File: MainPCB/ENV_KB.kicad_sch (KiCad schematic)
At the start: 198 parts

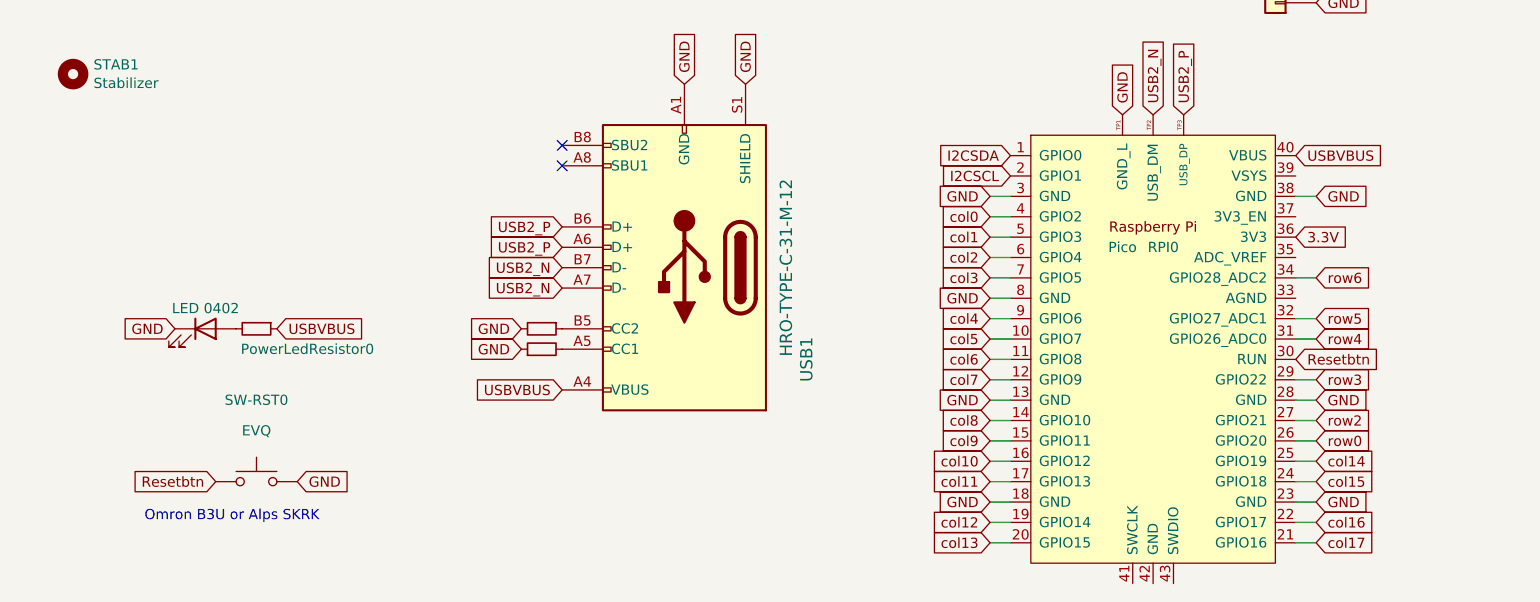
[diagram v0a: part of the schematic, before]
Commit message: swapped footprint of various parts, updated the logo and tweaked some traces
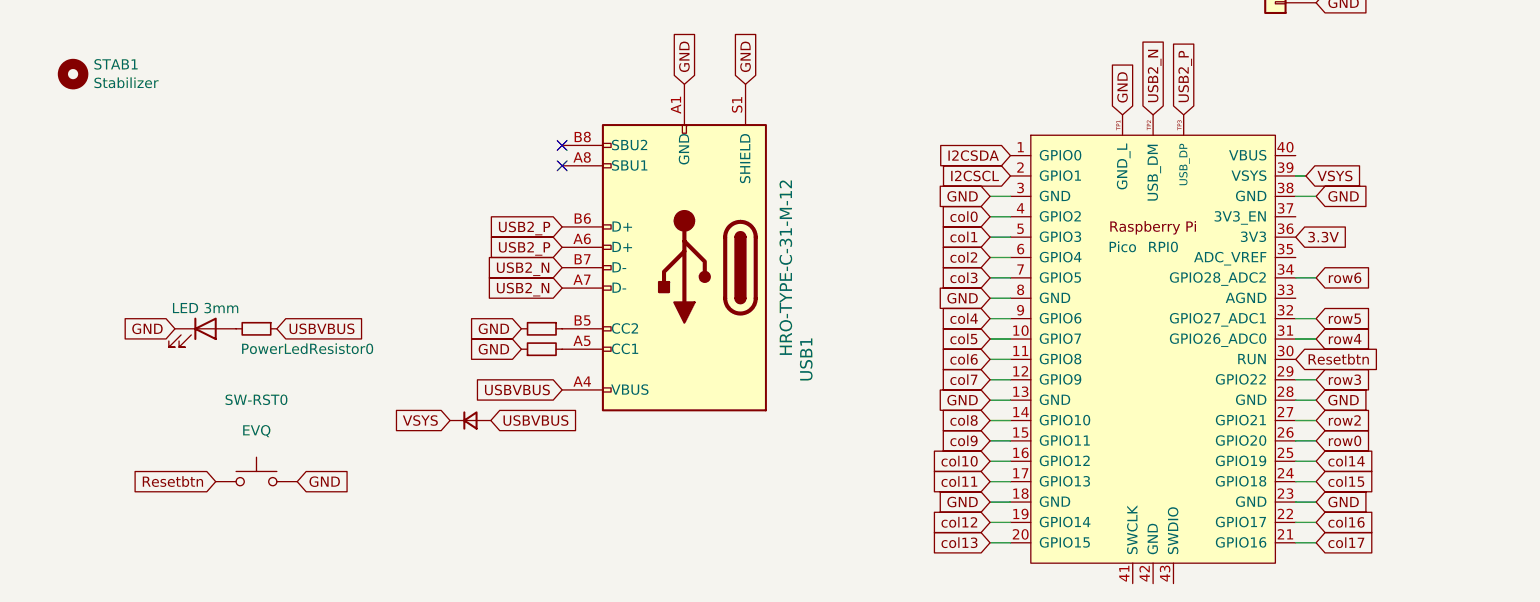
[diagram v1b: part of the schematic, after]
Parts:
- added D89: 1n4002, Diode_THT:D_DO-35_SOD27_P7.62mm_Horizontal, symbol Device:D_Small
- PowerLED0: value LED 0402 -> LED 3mm; footprint LED_SMD:LED_0402_1005Metric -> LED_THT:LED_D3.0mm
- PowerLedResistor0: value 47K Resistor 0402 -> 47K Resistor; footprint Resistor_SMD:R_0402_1005Metric -> Resistor_THT:R_Axial_DIN0207_L6.3mm_D2.5mm_P7.62mm_Horizontal
- RESISTOR0, RESISTOR1: value 5.1kohm 0402 -> 5.1k; footprint Resistor_SMD:R_0402_1005Metric -> Resistor_THT:R_Axial_DIN0207_L6.3mm_D2.5mm_P7.62mm_Horizontal
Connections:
- net USBVBUS: now also D89.2 (A); no longer RPI0.40 (VBUS)
- net VSYS: now reaches RPI0.39 (VSYS)
- net VSYS: now also D89.1 (K)
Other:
- note removed: "Omron B3U or Alps SKRK"
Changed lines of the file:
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@@
     (stroke (width 0) (type default) (color 0 0 0 0))
   )
+  (wire (pts (xy 346.71 233.68) (xy 347.98 233.68))
+    (stroke (width 0) (type default) (color 0 0 0 0))
+  )
   (wire (pts (xy 288.29 181.61) (xy 288.29 182.88))
     (stroke (width 0) (type default) (color 0 0 0 0))
@@
     (effects (font (size 1.27 1.27)) (justify left bottom))
   )
-  (text "Omron B3U or Alps SKRK" (at 203.2 276.86 0)
-    (effects (font (size 1.27 1.27)) (justify left bottom))
-  )
   (global_label "I2CSDA" (shape input) (at 349.25 204.47 0) (fields_autoplaced)
     (effects (font (size 1.27 1.27)) (justify left))
@@
     )
   )
+  (global_label "VSYS" (shape input) (at 347.98 233.68 0) (fields_autoplaced)
+    (effects (font (size 1.27 1.27)) (justify left))
+    (property "Intersheet References" "${INTERSHEET_REFS}" (id 0) (at 354.9004 233.6006 0)
+      (effects (font (size 1.27 1.27)) (justify left) hide)
+    )
+  )
   (global_label "col17" (shape input) (at 477.52 16.51 180) (fields_autoplaced)
     (effects (font (size 1.27 1.27)) (justify right))
@@
     )
   )
+  (global_label "VSYS" (shape input) (at 241.3 264.16 180) (fields_autoplaced)
+    (effects (font (size 1.27 1.27)) (justify right))
+    (property "Intersheet References" "${INTERSHEET_REFS}" (id 0) (at 234.3796 264.2394 0)
+      (effects (font (size 1.27 1.27)) (justify right) hide)
+    )
+  )
   (global_label "GND" (shape input) (at 222.25 271.78 0) (fields_autoplaced)
     (effects (font (size 1.27 1.27)) (justify left))
@@
     )
   )
-  (global_label "USBVBUS" (shape input) (at 346.71 231.14 0) (fields_autoplaced)
+  (global_label "USBVBUS" (shape input) (at 246.38 264.16 0) (fields_autoplaced)
     (effects (font (size 1.27 1.27)) (justify left))
-    (property "Intersheet References" "${INTERSHEET_REFS}" (id 0) (at 0 0 0)
+    (property "Intersheet References" "${INTERSHEET_REFS}" (id 0) (at -100.33 33.02 0)
       (effects (font (size 1.27 1.27)) hide)
     )
@@
       (effects (font (size 1.27 1.27)) hide)
     )
-    (property "Value" "LED 0402" (id 1) (at 210.82 250.19 0))
-    (property "Footprint" "LED_SMD:LED_0402_1005Metric" (id 2) (at 210.82 252.73 0)
+    (property "Value" "LED 3mm" (id 1) (at 210.82 250.19 0))
+    (property "Footprint" "LED_THT:LED_D3.0mm" (id 2) (at 210.82 252.73 0)
       (effects (font (size 1.27 1.27)) hide)
     )
@@
     (in_bom yes) (on_board yes)
     (property "Reference" "PowerLedResistor0" (id 0) (at 223.52 255.27 90))
-    (property "Value" "47K Resistor 0402" (id 1) (at 218.44 256.54 90)
+    (property "Value" "47K Resistor" (id 1) (at 218.44 256.54 90)
       (effects (font (size 1.27 1.27)) hide)
     )
-    (property "Footprint" "Resistor_SMD:R_0402_1005Metric" (id 2) (at 217.17 252.73 0)
+    (property "Footprint" "Resistor_THT:R_Axial_DIN0207_L6.3mm_D2.5mm_P7.62mm_Horizontal" (id 2) (at 217.17 252.73 0)
       (effects (font (size 1.27 1.27)) hide)
     )
@@
       (effects (font (size 0.9906 0.9906)) hide)
     )
-    (property "Value" "5.1kohm 0402" (id 1) (at 250.19 255.27 90)
+    (property "Value" "5.1k " (id 1) (at 250.19 255.27 90)
       (effects (font (size 0.762 0.762)) hide)
     )
-    (property "Footprint" "Resistor_SMD:R_0402_1005Metric" (id 2) (at 252.73 255.27 0)
+    (property "Footprint" "Resistor_THT:R_Axial_DIN0207_L6.3mm_D2.5mm_P7.62mm_Horizontal" (id 2) (at 252.73 255.27 0)
       (effects (font (size 1.27 1.27)) hide)
     )
@@
       (effects (font (size 0.9906 0.9906)) hide)
     )
-    (property "Value" "5.1kohm 0402" (id 1) (at 252.73 250.063 90)
+    (property "Value" "5.1k" (id 1) (at 252.73 250.063 90)
       (effects (font (size 1.27 1.27)) hide)
     )
-    (property "Footprint" "Resistor_SMD:R_0402_1005Metric" (id 2) (at 252.73 252.73 0)
+    (property "Footprint" "Resistor_THT:R_Axial_DIN0207_L6.3mm_D2.5mm_P7.62mm_Horizontal" (id 2) (at 252.73 252.73 0)
       (effects (font (size 1.27 1.27)) hide)
     )
@@
     (pin "2")
   )
+  (symbol (lib_id "Device:D_Small") (at 243.84 264.16 0) (unit 1)
+    (in_bom yes) (on_board yes) (fields_autoplaced)
+    (property "Reference" "D89" (id 0) (at 243.84 257.81 0)
+      (effects (font (size 1.27 1.27)) hide)
+    )
+    (property "Value" "1n4002" (id 1) (at 243.84 260.35 0)
+      (effects (font (size 1.27 1.27)) hide)
+    )
+    (property "Footprint" "Diode_THT:D_DO-35_SOD27_P7.62mm_Horizontal" (id 2) (at 243.84 264.16 90)
+      (effects (font (size 1.27 1.27)) hide)
+    )
+    (property "Datasheet" "~" (id 3) (at 243.84 264.16 90)
+      (effects (font (size 1.27 1.27)) hide)
+    )
+    (pin "1")
+    (pin "2")
+  )
   (sheet_instances
     (path "/" (page "1"))
@@
       (reference "D88") (unit 1) (value "D") (footprint "Diode_THT:D_DO-35_SOD27_P7.62mm_Horizontal")
     )
+    (path "/8b8c9314-8d61-4cdd-87d9-99f8c66c7b75"
+      (reference "D89") (unit 1) (value "1n4002") (footprint "Diode_THT:D_DO-35_SOD27_P7.62mm_Horizontal")
+    )
     (path "/00000000-0000-0000-0000-0000605938c3"
       (reference "H0") (unit 1) (value "MountingHole") (footprint "MountingHole:MountingHole_2.2mm_M2_Pad")
@@
     )
     (path "/00000000-0000-0000-0000-00006043f14d"
-      (reference "PowerLED0") (unit 1) (value "LED 0402") (footprint "LED_SMD:LED_0402_1005Metric")
+      (reference "PowerLED0") (unit 1) (value "LED 3mm") (footprint "LED_THT:LED_D3.0mm")
     )
     (path "/00000000-0000-0000-0000-0000604a80b1"
-      (reference "PowerLedResistor0") (unit 1) (value "47K Resistor 0402") (footprint "Resistor_SMD:R_0402_1005Metric")
+      (reference "PowerLedResistor0") (unit 1) (value "47K Resistor") (footprint "Resistor_THT:R_Axial_DIN0207_L6.3mm_D2.5mm_P7.62mm_Horizontal")
     )
     (path "/00000000-0000-0000-0000-00006066af89"
-      (reference "RESISTOR0") (unit 1) (value "5.1kohm 0402") (footprint "Resistor_SMD:R_0402_1005Metric")
+      (reference "RESISTOR0") (unit 1) (value "5.1k") (footprint "Resistor_THT:R_Axial_DIN0207_L6.3mm_D2.5mm_P7.62mm_Horizontal")
     )
     (path "/00000000-0000-0000-0000-0000606333e5"
-      (reference "RESISTOR1") (unit 1) (value "5.1kohm 0402") (footprint "Resistor_SMD:R_0402_1005Metric")
+      (reference "RESISTOR1") (unit 1) (value "5.1k ") (footprint "Resistor_THT:R_Axial_DIN0207_L6.3mm_D2.5mm_P7.62mm_Horizontal")
     )
     (path "/00000000-0000-0000-0000-0000604d8043"

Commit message: Added Stepped left shift for orig version
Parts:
- added K_50A1: KEYSW, MX_Only:MXOnly-1.25U-NoLED, symbol MX_Alps_Hybrid:MX-NoLED
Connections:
- net col0: now also K_50A1.1 (COL)
- net at D50.2 (A), K_50.2 (ROW): now also K_50A1.2 (ROW)
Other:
- note added: "Stepped capslock"
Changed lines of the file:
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@@
   (junction (at 299.72 24.13) (diameter 0) (color 0 0 0 0)
   )
+  (junction (at 34.29 130.81) (diameter 0) (color 0 0 0 0)
+  )
   (junction (at 364.49 111.76) (diameter 0) (color 0 0 0 0)
   )
@@
   (junction (at 186.69 86.36) (diameter 0) (color 0 0 0 0)
   )
+  (junction (at 39.37 125.73) (diameter 0) (color 0 0 0 0)
+  )
   (no_connect (at 255.27 229.87))
   (no_connect (at 255.27 232.41))
@@
     (stroke (width 0) (type default) (color 0 0 0 0))
   )
+  (wire (pts (xy 31.75 130.81) (xy 34.29 130.81))
+    (stroke (width 0) (type default) (color 0 0 0 0))
+  )
   (wire (pts (xy 299.72 151.13) (xy 299.72 125.73))
     (stroke (width 0) (type default) (color 0 0 0 0))
@@
     (stroke (width 0) (type default) (color 0 0 0 0))
   )
+  (wire (pts (xy 39.37 123.19) (xy 39.37 125.73))
+    (stroke (width 0) (type default) (color 0 0 0 0))
+  )
   (wire (pts (xy 237.49 130.81) (xy 237.49 132.08))
     (stroke (width 0) (type default) (color 0 0 0 0))
@@
     (stroke (width 0) (type default) (color 0 0 0 0))
   )
+  (wire (pts (xy 36.83 123.19) (xy 39.37 123.19))
+    (stroke (width 0) (type default) (color 0 0 0 0))
+  )
   (wire (pts (xy 440.69 105.41) (xy 440.69 106.68))
     (stroke (width 0) (type default) (color 0 0 0 0))
@@
     (stroke (width 0) (type default) (color 0 0 0 0))
   )
+  (wire (pts (xy 31.75 128.27) (xy 31.75 130.81))
+    (stroke (width 0) (type default) (color 0 0 0 0))
+  )
   (wire (pts (xy 452.12 16.51) (xy 452.12 24.13))
     (stroke (width 0) (type default) (color 0 0 0 0))
@@
     (effects (font (size 1.27 1.27)) (justify left bottom))
   )
+  (text "Stepped capslock\n" (at 13.97 130.81 0)
+    (effects (font (size 1.27 1.27)) (justify left bottom))
+  )
   (global_label "I2CSDA" (shape input) (at 349.25 204.47 0) (fields_autoplaced)
     (effects (font (size 1.27 1.27)) (justify left))
@@
     (pin "2")
   )
+  (symbol (lib_id "MX_Alps_Hybrid:MX-NoLED") (at 33.02 124.46 0) (unit 1)
+    (in_bom yes) (on_board yes)
+    (property "Reference" "K_50A1" (id 0) (at 33.02 118.5418 0)
+      (effects (font (size 1.524 1.524)))
+    )
+    (property "Value" "KEYSW" (id 1) (at 33.02 127 0)
+      (effects (font (size 1.524 1.524)) hide)
+    )
+    (property "Footprint" "MX_Only:MXOnly-1.25U-NoLED" (id 2) (at 33.02 124.46 0)
+      (effects (font (size 1.524 1.524)) hide)
+    )
+    (property "Datasheet" "" (id 3) (at 33.02 124.46 0)
+      (effects (font (size 1.524 1.524)))
+    )
+    (pin "1")
+    (pin "2")
+  )
   (sheet_instances
     (path "/" (page "1"))
@@
       (reference "K_50") (unit 1) (value "KEYSW") (footprint "MX_Only:MXOnly-1.75U-NoLED")
     )
+    (path "/fd5e4835-336e-4184-bf66-faee23f94ad4"
+      (reference "K_50A1") (unit 1) (value "KEYSW") (footprint "MX_Only:MXOnly-1.25U-NoLED")
+    )
     (path "/00000000-0000-0000-0000-000000000511"

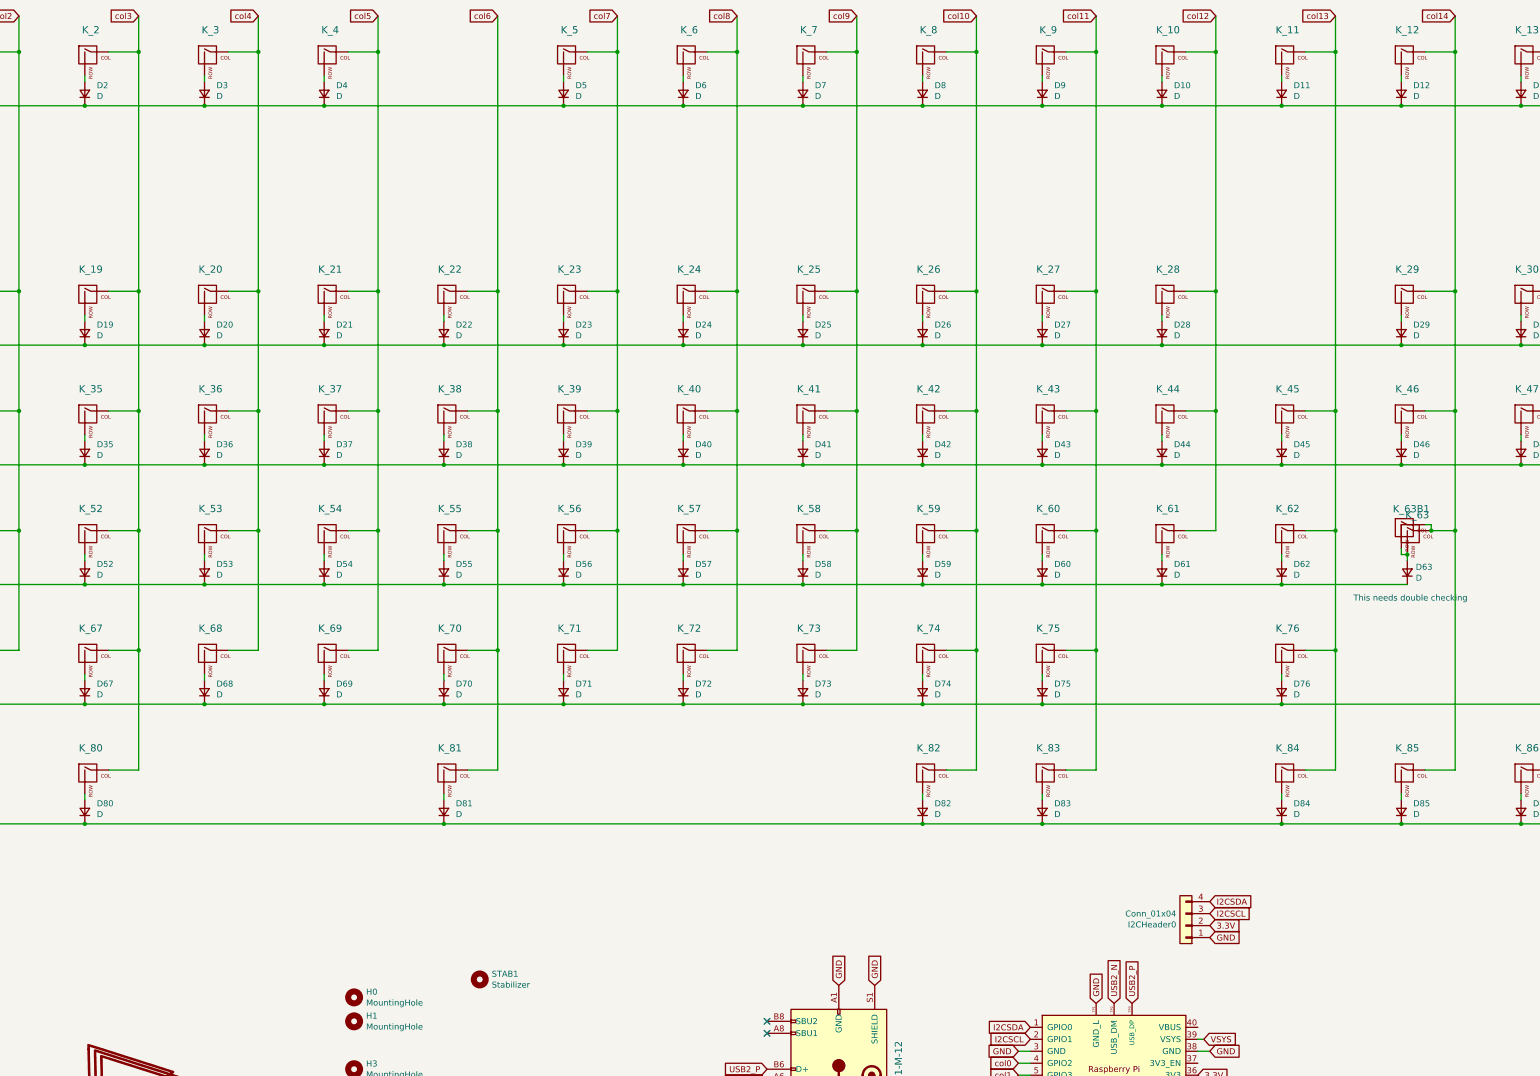
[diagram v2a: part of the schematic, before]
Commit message: Added split space and split backspace.
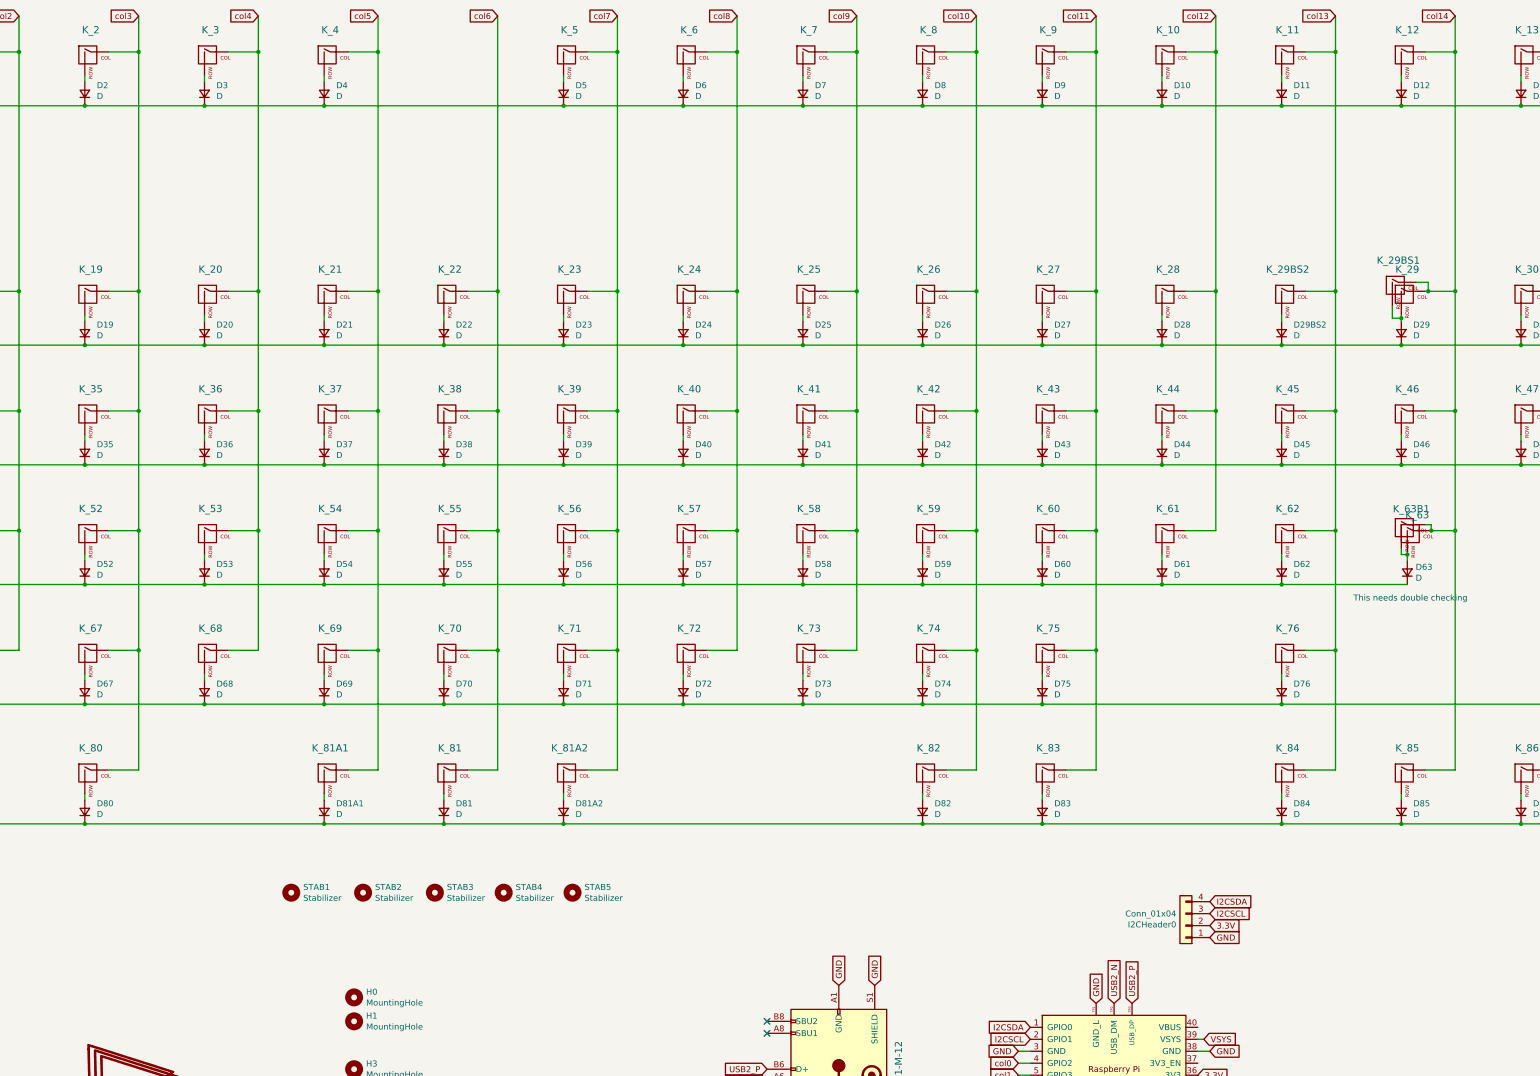
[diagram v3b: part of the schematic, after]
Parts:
- added D29BS2, D81A1, D81A2: D, Diode_THT:D_DO-35_SOD27_P7.62mm_Horizontal, symbol Device:D_Small
- added K_29BS1, K_29BS2, K_81A1, K_81A2: KEYSW, MX_Only:MXOnly-1U-NoLED, symbol MX_Alps_Hybrid:MX-NoLED
- added STAB2, STAB3, STAB4, STAB5: Stabilizer, Mounting_Keyboard_Stabilizer:Stabilizer_Cherry_MX_2u, symbol Mechanical:MountingHole
- K_29: footprint MX_Only:MXOnly-2U-NoLED -> MX_Only:MXOnly-1U-NoLED
- K_81: footprint MX_Only:MXOnly-6.25U-ReversedStabilizers-NoLED -> MX_Only:MXOnly-1U-NoLED
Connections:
- net col13: now also K_29BS2.1 (COL)
- net col14: now also K_29BS1.1 (COL)
- net col5: now also K_81A1.1 (COL)
- net col7: now also K_81A2.1 (COL)
- net row2: now also D29BS2.1 (K)
- net row6: now also D81A1.1 (K), D81A2.1 (K)
- net at D29.2 (A), K_29.2 (ROW): now also K_29BS1.2 (ROW)
- new net: D29BS2.2 (A), K_29BS2.2 (ROW)
- new net: D81A2.2 (A), K_81A2.2 (ROW)
- new net: D81A1.2 (A), K_81A1.2 (ROW)
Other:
- moved on the sheet: STAB1

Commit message: tiny tweaks
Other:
- note removed: "This needs double checking"
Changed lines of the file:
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@@
     (stroke (width 0) (type default) (color 0 0 0 0))
-  )
-  (text "This needs double checking" (at 379.73 140.97 0)
-    (effects (font (size 1.27 1.27)) (justify left bottom))
   )
   (text "Stepped capslock\n" (at 13.97 130.81 0)
